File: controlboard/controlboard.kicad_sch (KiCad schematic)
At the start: 32 parts, among them J10 Conn_01x02_Pin, J27 GPIO, J6 Conn_02x04_Counter_Clockwise, SW2 SW_Push TODO FP CHECK

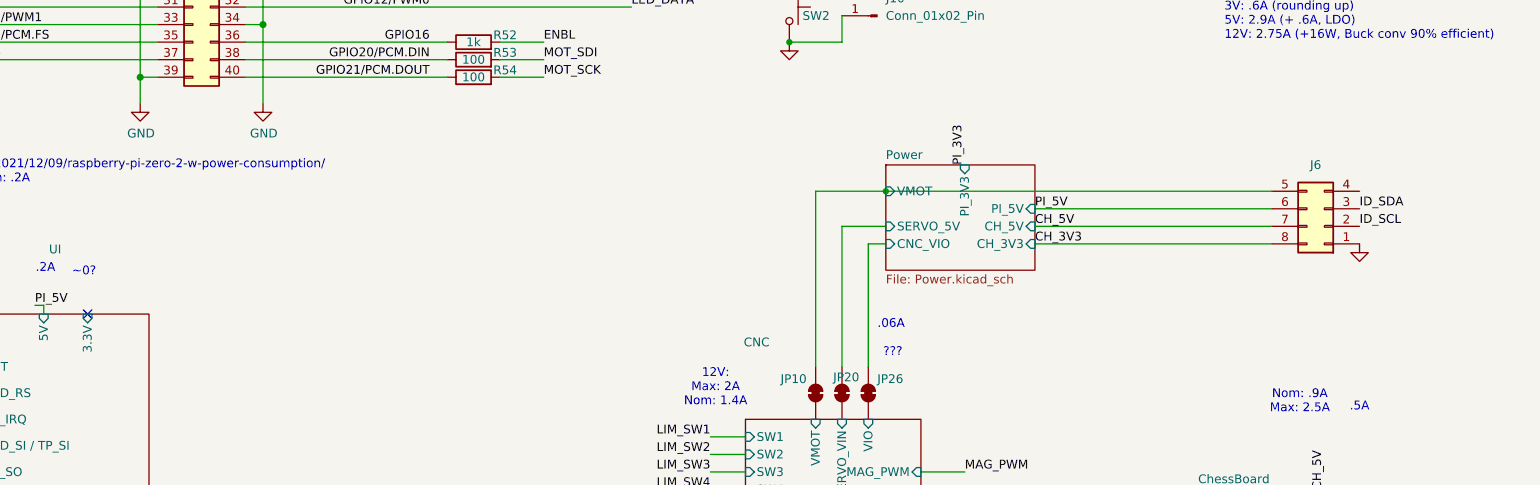
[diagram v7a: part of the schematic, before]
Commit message: improve pinout
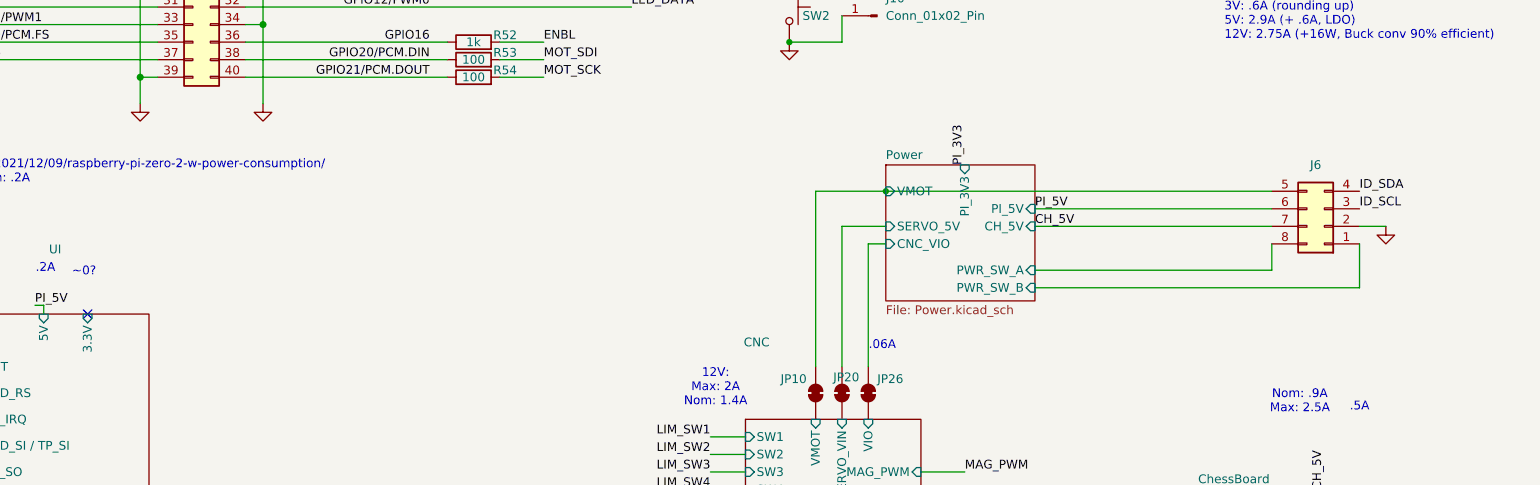
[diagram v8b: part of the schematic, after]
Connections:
- net GND: now also J6.2 (Pin_2); no longer J6.1 (Pin_1)
- net ID_SCL: now also J6.3 (Pin_3); no longer J6.2 (Pin_2)
- net ID_SDA: now also J6.4 (Pin_4); no longer J6.3 (Pin_3)
- net CH_3V3 renamed Power/PWR_SW_A
- new net Power/PWR_SW_B: J6.1 (Pin_1)
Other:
- sheet Power ports: added PWR_SW_A, PWR_SW_B; removed CH_3V3
- note removed: "???"
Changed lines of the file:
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@@
 	(wire
 		(pts
+			(xy 259.08 101.6) (xy 259.08 95.25)
+		)
+		(stroke
+			(width 0)
+			(type default)
+		)
+	)
+	(wire
+		(pts
 			(xy 134.62 35.56) (xy 140.97 35.56)
 		)
@@
 	(wire
 		(pts
+			(xy 246.38 99.06) (xy 246.38 95.25)
+		)
+		(stroke
+			(width 0)
+			(type default)
+		)
+	)
+	(wire
+		(pts
 			(xy 97.79 33.02) (xy 127 33.02)
 		)
@@
 	(wire
 		(pts
-			(xy 212.09 95.25) (xy 246.38 95.25)
-		)
-		(stroke
-			(width 0)
-			(type default)
-		)
-	)
-	(wire
-		(pts
 			(xy 100.33 27.94) (xy 97.79 27.94)
 		)
@@
 	(wire
 		(pts
+			(xy 212.09 101.6) (xy 259.08 101.6)
+		)
+		(stroke
+			(width 0)
+			(type default)
+		)
+	)
+	(wire
+		(pts
 			(xy 195.58 132.08) (xy 201.93 132.08)
 		)
@@
 	(wire
 		(pts
+			(xy 212.09 99.06) (xy 246.38 99.06)
+		)
+		(stroke
+			(width 0)
+			(type default)
+		)
+	)
+	(wire
+		(pts
 			(xy 212.09 92.71) (xy 246.38 92.71)
 		)
@@
 	(wire
 		(pts
+			(xy 259.08 92.71) (xy 262.89 92.71)
+		)
+		(stroke
+			(width 0)
+			(type default)
+		)
+	)
+	(wire
+		(pts
 			(xy 68.58 104.14) (xy 68.58 105.41)
 		)
@@
 	(text ".06A"
 		(exclude_from_sim no)
-		(at 191.262 106.934 0)
+		(at 189.992 109.982 0)
 		(effects
 			(font
@@
 		)
 	)
-	(text "???"
-		(exclude_from_sim no)
-		(at 191.516 110.998 0)
-		(effects
-			(font
-				(size 1.27 1.27)
-			)
-		)
-	)
 	(text "Soft shutdown button"
 		(exclude_from_sim no)
@@
 		)
 	)
-	(label "ID_SCL"
-		(at 259.08 92.71 0)
-		(fields_autoplaced yes)
-		(effects
-			(font
-				(size 1.27 1.27)
-			)
-			(justify left bottom)
-		)
-	)
 	(label "GPIO27"
 		(at 55.88 38.1 0)
@@
 		)
 	)
+	(label "ID_SDA"
+		(at 259.08 87.63 0)
+		(fields_autoplaced yes)
+		(effects
+			(font
+				(size 1.27 1.27)
+			)
+			(justify left bottom)
+		)
+	)
 	(label "TP_SO"
 		(at 58.42 128.27 180)
@@
 		)
 	)
-	(label "ID_SDA"
-		(at 259.08 90.17 0)
-		(fields_autoplaced yes)
-		(effects
-			(font
-				(size 1.27 1.27)
-			)
-			(justify left bottom)
-		)
-	)
 	(label "GPIO6"
 		(at 55.88 60.96 0)
@@
 		)
 	)
-	(label "CH_3V3"
-		(at 212.09 95.25 0)
-		(fields_autoplaced yes)
-		(effects
-			(font
-				(size 1.27 1.27)
-			)
-			(justify left bottom)
-		)
-	)
 	(label "GPIO4{slash}GPCLK0"
 		(at 55.88 30.48 0)
@@
 		)
 	)
+	(label "ID_SCL"
+		(at 259.08 90.17 0)
+		(fields_autoplaced yes)
+		(effects
+			(font
+				(size 1.27 1.27)
+			)
+			(justify left bottom)
+		)
+	)
 	(label "PI_5V"
 		(at 100.33 19.05 0)
@@
 	)
 	(symbol
-		(lib_id "power:GND")
-		(at 259.08 95.25 0)
-		(unit 1)
-		(exclude_from_sim no)
-		(in_bom yes)
-		(on_board yes)
-		(dnp no)
-		(property "Reference" "#PWR031"
-			(at 259.08 101.6 0)
-			(effects
-				(font
-					(size 1.27 1.27)
-				)
-				(hide yes)
-			)
-		)
-		(property "Value" "GND"
-			(at 259.1943 99.5744 0)
-			(effects
-				(font
-					(size 1.27 1.27)
-				)
-				(hide yes)
-			)
-		)
-		(property "Footprint" ""
-			(at 259.08 95.25 0)
-			(effects
-				(font
-					(size 1.27 1.27)
-				)
-			)
-		)
-		(property "Datasheet" ""
-			(at 259.08 95.25 0)
-			(effects
-				(font
-					(size 1.27 1.27)
-				)
-			)
-		)
-		(property "Description" ""
-			(at 259.08 95.25 0)
-			(effects
-				(font
-					(size 1.27 1.27)
-				)
-				(hide yes)
-			)
-		)
-		(pin "1"
-		)
-		(instances
-			(project "controlboard"
-				(path "/2797250d-6fee-4769-b4dd-0e20ce4f0941"
-					(reference "#PWR031")
-					(unit 1)
-				)
-			)
-		)
-	)
-	(symbol
 		(lib_id "Jumper:Jumper_2_Bridged")
 		(at 158.75 146.05 0)
@@
 	)
 	(symbol
+		(lib_id "power:GND")
+		(at 262.89 92.71 0)
+		(unit 1)
+		(exclude_from_sim no)
+		(in_bom yes)
+		(on_board yes)
+		(dnp no)
+		(property "Reference" "#PWR05"
+			(at 262.89 99.06 0)
+			(effects
+				(font
+					(size 1.27 1.27)
+				)
+				(hide yes)
+			)
+		)
+		(property "Value" "GND"
+			(at 263.0043 97.0344 0)
+			(effects
+				(font
+					(size 1.27 1.27)
+				)
+				(hide yes)
+			)
+		)
+		(property "Footprint" ""
+			(at 262.89 92.71 0)
+			(effects
+				(font
+					(size 1.27 1.27)
+				)
+			)
+		)
+		(property "Datasheet" ""
+			(at 262.89 92.71 0)
+			(effects
+				(font
+					(size 1.27 1.27)
+				)
+			)
+		)
+		(property "Description" ""
+			(at 262.89 92.71 0)
+			(effects
+				(font
+					(size 1.27 1.27)
+				)
+				(hide yes)
+			)
+		)
+		(pin "1"
+		)
+		(instances
+			(project "controlboard"
+				(path "/2797250d-6fee-4769-b4dd-0e20ce4f0941"
+					(reference "#PWR05")
+					(unit 1)
+				)
+			)
+		)
+	)
+	(symbol
 		(lib_id "Device:R")
 		(at 130.81 68.58 90)
@@
 					(size 1.27 1.27)
 				)
+				(hide yes)
 			)
 		)
@@
 					(size 1.27 1.27)
 				)
+				(hide yes)
 			)
 		)
@@
 	(sheet
 		(at 190.5 83.82)
-		(size 21.59 15.24)
+		(size 21.59 19.685)
 		(fields_autoplaced yes)
 		(stroke
@@
 		)
 		(property "Sheetfile" "Power.kicad_sch"
-			(at 190.5 99.6446 0)
+			(at 190.5 104.0896 0)
 			(effects
 				(font
@@
 			)
 		)
-		(pin "CH_3V3" input
-			(at 212.09 95.25 0)
-			(effects
-				(font
-					(size 1.27 1.27)
-				)
-				(justify right)
-			)
-		)
 		(pin "PI_5V" input
 			(at 212.09 90.17 0)
@@
 			(effects
 				(font
+					(size 1.27 1.27)
+				)
+				(justify right)
+			)
+		)
+		(pin "PWR_SW_B" input
+			(at 212.09 101.6 0)
+			(effects
+				(font
+					(size 1.27 1.27)
+				)
+				(justify right)
+			)
+		)
+		(pin "PWR_SW_A" input
+			(at 212.09 99.06 0)
+			(effects
+				(font
